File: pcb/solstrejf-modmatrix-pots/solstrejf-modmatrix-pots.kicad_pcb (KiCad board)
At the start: 2 copper layers, 165.1 x 246.9 mm, 58 parts, among them J1 Conn_02x08_Counter_Clockwise, J2 Conn_02x08_Counter_Clockwise, J3 Conn_02x08_Counter_Clockwise, J4 Conn_02x08_Counter_Clockwise

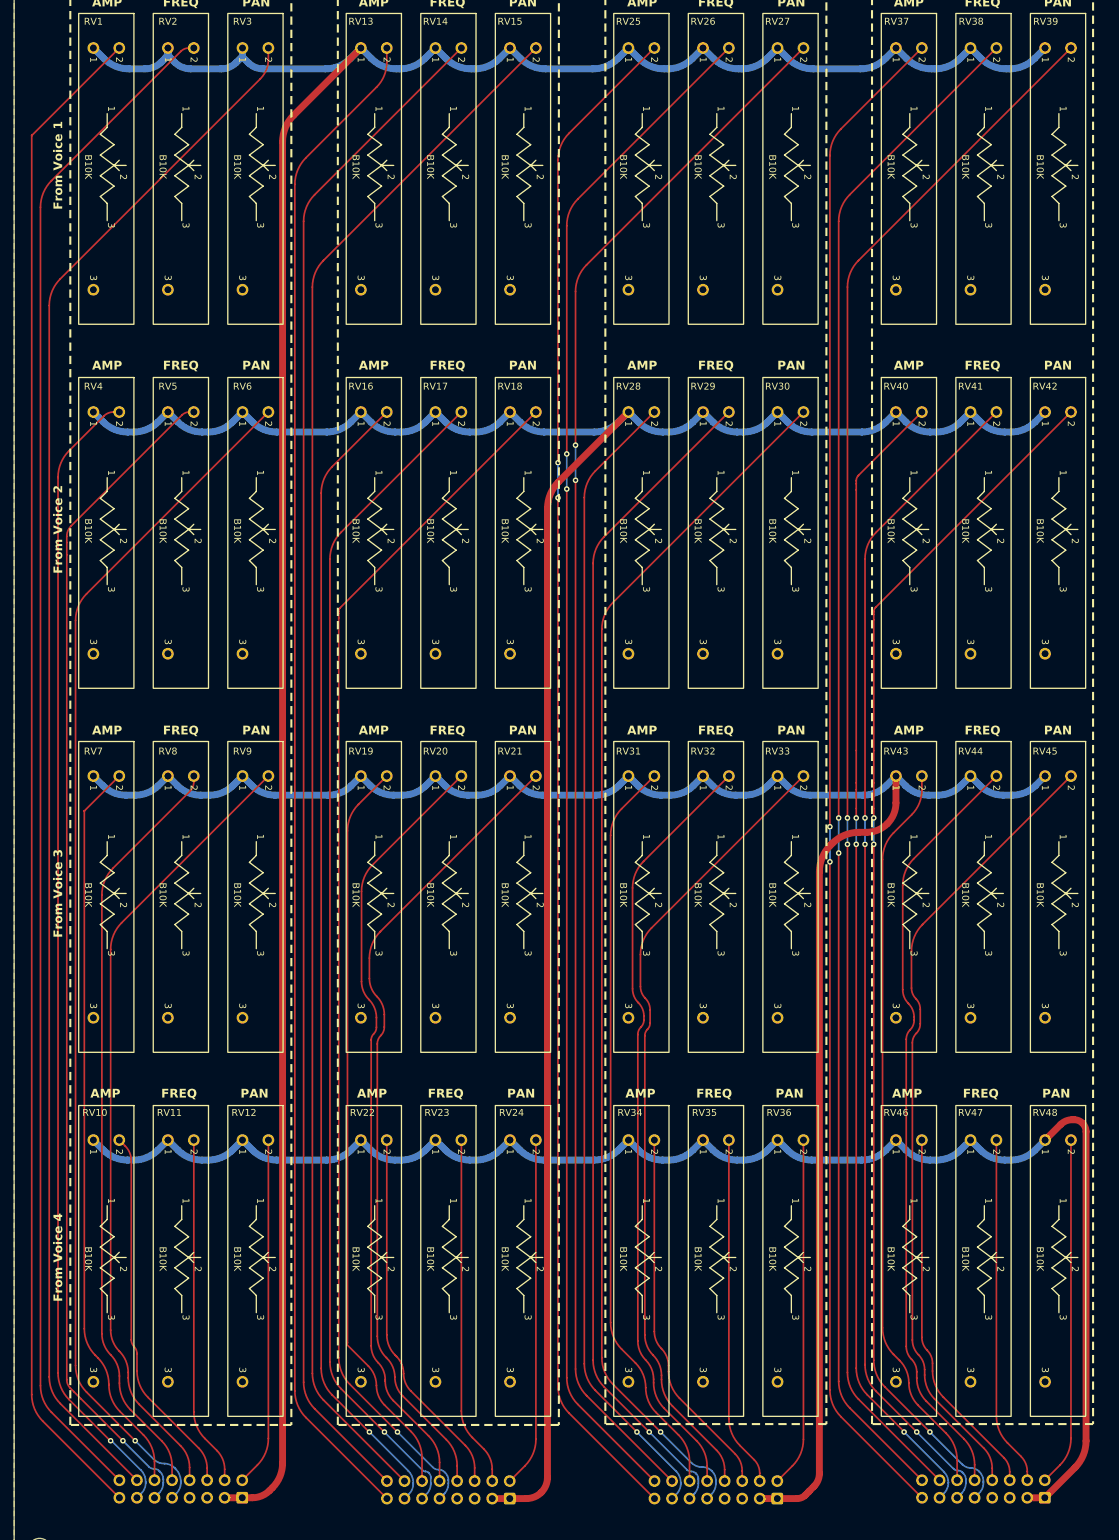
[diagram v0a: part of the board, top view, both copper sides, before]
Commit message: updated Alpha slide pot footprint to have 1.2mm drill hole diameter to match the 1mm pins
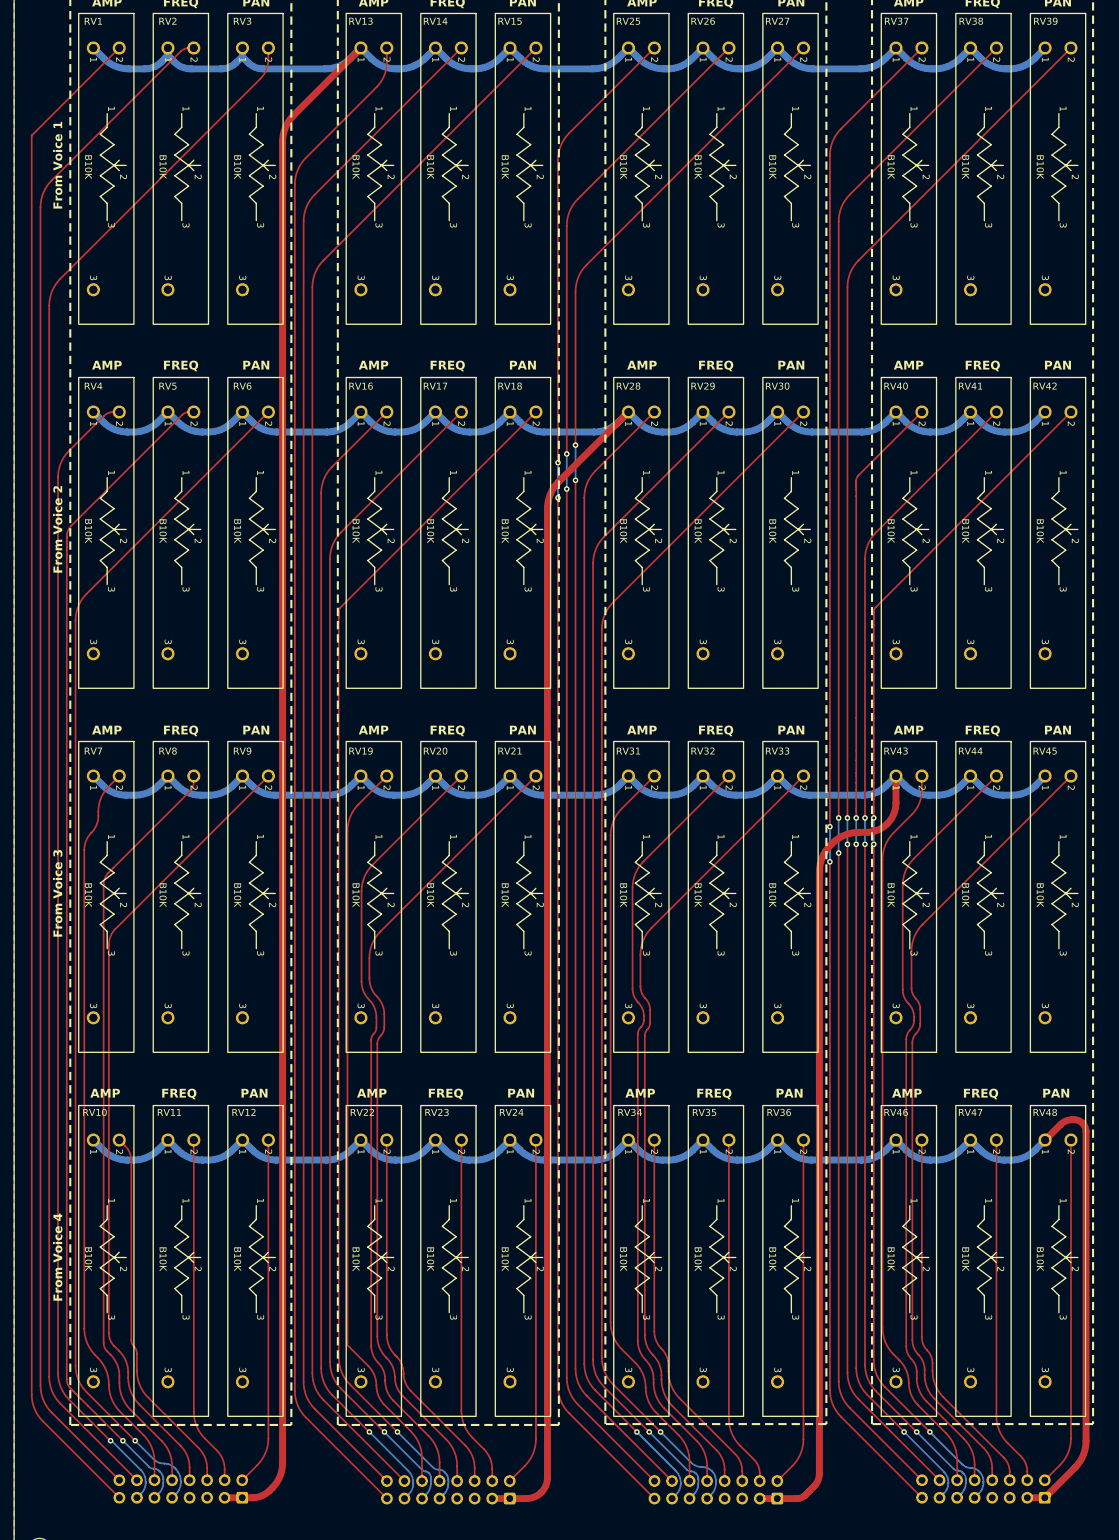
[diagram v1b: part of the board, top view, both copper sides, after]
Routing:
- net /V1AMP3: track 107.2 -> 106.6 mm

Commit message: Added variable revision and date silkscreen prints for all four boards of Solstrejf
This means that the revision and issue date that is set in the page setup
of the PCB's will be update on the silscreen automatically so I don't forget
to update the revsions on the silkscreen :')
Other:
- board text added: "Kromftronics // Solfstrejf ModMatrix Rev ${REVISION}"
- board text removed: "Kromftronics // Solfstrejf ModMatrix Rev 1.0"
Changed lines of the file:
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@@
 		)
 	)
-	(gr_text "Kromftronics // Solfstrejf ModMatrix Rev 1.0"
+	(gr_text "Kromftronics // Solfstrejf ModMatrix Rev ${REVISION}"
 		(at 64.897 53.860954 0)
 		(layer "B.SilkS")
